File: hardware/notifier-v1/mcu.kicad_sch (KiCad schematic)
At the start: 18 parts, among them SW1 RESET, SW2 BOOT, SW3 BUTTON, U1 ESP32-S3-WROOM-1-N8R2

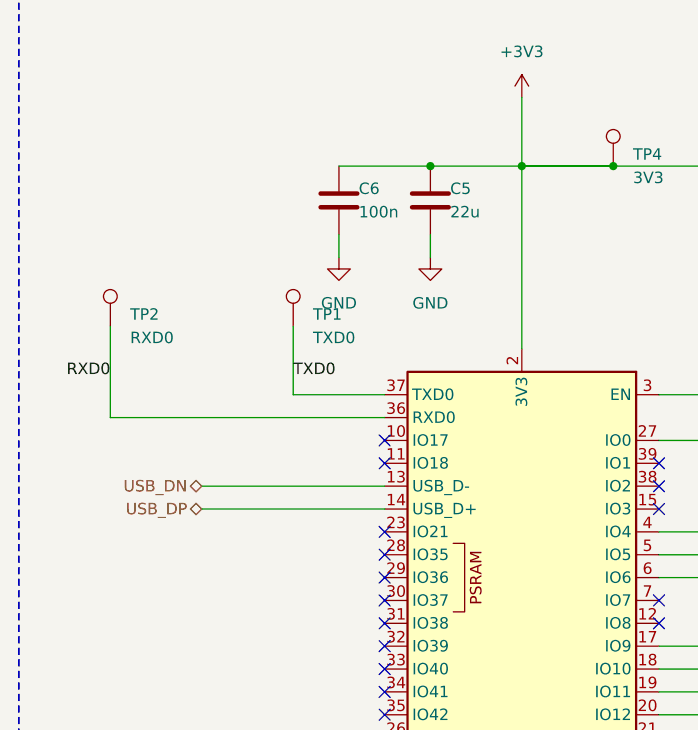
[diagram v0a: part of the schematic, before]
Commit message: notifier-v1: USB 22 ohm series resistors, 1 uF at module 3V3, second buck output cap
Co-Authored-By: Claude Opus 5.5 <noreply@anthropic.com>
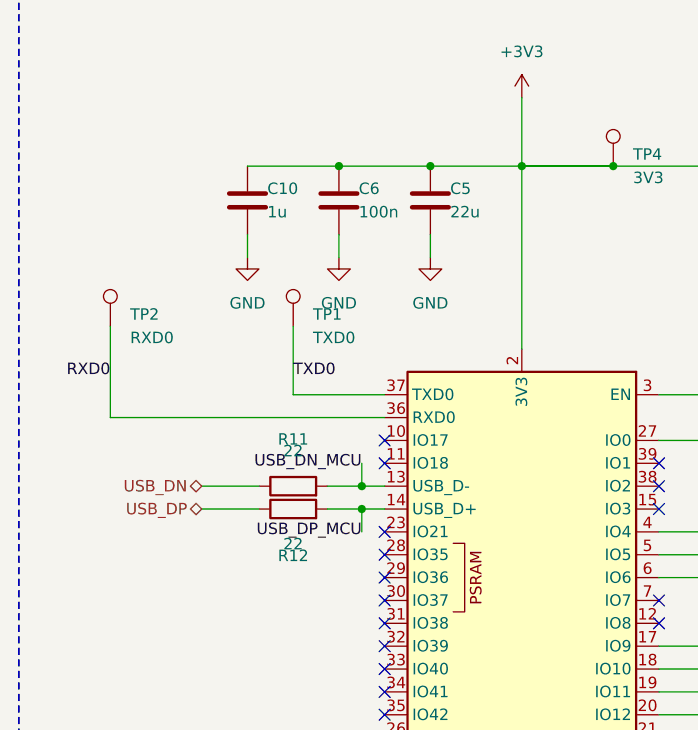
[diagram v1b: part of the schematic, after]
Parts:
- added C10: 1u, Capacitor_SMD:C_0402_1005Metric, symbol Device:C
- added R11, R12: 22, Resistor_SMD:R_0402_1005Metric, symbol Device:R
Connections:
- net +3V3: now also C10.1
- net GND: now also C10.2
- net USB_DN: now also R11.1; no longer U1.13 (USB_D-)
- net USB_DP: now also R12.1; no longer U1.14 (USB_D+)
- new net USB_DN_MCU: R11.2, U1.13 (USB_D-)
- new net USB_DP_MCU: R12.2, U1.14 (USB_D+)
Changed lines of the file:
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@@
+	)
+	(symbol
+		(lib_id "Device:C")
+		(at 172.72 95.25 0)
+		(unit 1)
+		(exclude_from_sim no)
+		(in_bom yes)
+		(on_board yes)
+		(dnp no)
+		(fields_autoplaced no)
+		(property "Reference" "C10"
+			(at 174.92 93.95 0)
+			(effects
+				(font
+					(size 1.27 1.27)
+				) (justify left)
+			)
+		)
+		(property "Value" "1u"
+			(at 174.92 96.55 0)
+			(effects
+				(font
+					(size 1.27 1.27)
+				) (justify left)
+			)
+		)
+		(property "Footprint" "Capacitor_SMD:C_0402_1005Metric"
+			(at 173.6852 91.44 0.0000)
+			(effects
+				(font
+					(size 1.27 1.27)
+				)
+				(hide yes)
+			)
+		)
+		(property "LCSC" "C52923"
+			(at 175.26 100.3299 0)
+			(effects
+				(font
+					(size 1.27 1.27)
+				)
+				(justify left) (hide yes)
+			)
+		)
+		(pin "1"
+		)
+		(pin "2"
+		)
+		(instances
+			(project "notifier-v1"
+				(path "/85cf2753-6181-5f74-b525-c66aecc4c100/8ee93a8b-7827-5c2b-aac9-b7bd720c2d76"
+					(reference "C10")
+					(unit 1)
+				)
+			)
+		)
+	)
+	(symbol
+		(lib_id "power:GND")
+		(at 172.72 101.6 0)
+		(unit 1)
+		(exclude_from_sim no)
+		(in_bom yes)
+		(on_board yes)
+		(dnp no)
+		(fields_autoplaced no)
+		(property "Reference" "#PWR15"
+			(at 172.72 95.25 0.0000)
+			(effects
+				(font
+					(size 1.27 1.27)
+				)
+				(justify left)
+				(hide yes)
+			)
+		)
+		(property "Value" "GND"
+			(at 172.72 106.68 0)
+			(effects
+				(font
+					(size 1.27 1.27)
+				)
+			)
+		)
+		(pin "1"
+		)
+		(instances
+			(project "notifier-v1"
+				(path "/85cf2753-6181-5f74-b525-c66aecc4c100/8ee93a8b-7827-5c2b-aac9-b7bd720c2d76"
+					(reference "#PWR15")
+					(unit 1)
+				)
+			)
+		)
 	)
 	(symbol
@@
 		(dnp no)
 		(fields_autoplaced no)
-		(property "Reference" "#PWR15"
+		(property "Reference" "#PWR16"
 			(at 203.2 171.45 0.0000)
 			(effects
@@
 			(project "notifier-v1"
 				(path "/85cf2753-6181-5f74-b525-c66aecc4c100/8ee93a8b-7827-5c2b-aac9-b7bd720c2d76"
-					(reference "#PWR15")
+					(reference "#PWR16")
 					(unit 1)
 				)
@@
 	)
 	(symbol
+		(lib_id "Device:R")
+		(at 177.8 127 90)
+		(unit 1)
+		(exclude_from_sim no)
+		(in_bom yes)
+		(on_board yes)
+		(dnp no)
+		(fields_autoplaced no)
+		(property "Reference" "R11"
+			(at 177.8 121.8 270)
+			(effects
+				(font
+					(size 1.27 1.27)
+				)
+			)
+		)
+		(property "Value" "22"
+			(at 177.8 123.1 270)
+			(effects
+				(font
+					(size 1.27 1.27)
+				)
+			)
+		)
+		(property "Footprint" "Resistor_SMD:R_0402_1005Metric"
+			(at 176.022 127 90)
+			(effects
+				(font
+					(size 1.27 1.27)
+				)
+				(hide yes)
+			)
+		)
+		(property "LCSC" "C25092"
+			(at 180.34 132.0799 0)
+			(effects
+				(font
+					(size 1.27 1.27)
+				)
+				(justify left) (hide yes)
+			)
+		)
+		(pin "1"
+		)
+		(pin "2"
+		)
+		(instances
+			(project "notifier-v1"
+				(path "/85cf2753-6181-5f74-b525-c66aecc4c100/8ee93a8b-7827-5c2b-aac9-b7bd720c2d76"
+					(reference "R11")
+					(unit 1)
+				)
+			)
+		)
+	)
+	(symbol
+		(lib_id "Device:R")
+		(at 177.8 129.54 90)
+		(unit 1)
+		(exclude_from_sim no)
+		(in_bom yes)
+		(on_board yes)
+		(dnp no)
+		(fields_autoplaced no)
+		(property "Reference" "R12"
+			(at 177.8 134.74 270)
+			(effects
+				(font
+					(size 1.27 1.27)
+				)
+			)
+		)
+		(property "Value" "22"
+			(at 177.8 133.44 270)
+			(effects
+				(font
+					(size 1.27 1.27)
+				)
+			)
+		)
+		(property "Footprint" "Resistor_SMD:R_0402_1005Metric"
+			(at 176.022 129.54 90)
+			(effects
+				(font
+					(size 1.27 1.27)
+				)
+				(hide yes)
+			)
+		)
+		(property "LCSC" "C25092"
+			(at 180.34 134.6199 0)
+			(effects
+				(font
+					(size 1.27 1.27)
+				)
+				(justify left) (hide yes)
+			)
+		)
+		(pin "1"
+		)
+		(pin "2"
+		)
+		(instances
+			(project "notifier-v1"
+				(path "/85cf2753-6181-5f74-b525-c66aecc4c100/8ee93a8b-7827-5c2b-aac9-b7bd720c2d76"
+					(reference "R12")
+					(unit 1)
+				)
+			)
+		)
+	)
+	(symbol
 		(lib_id "Connector:TestPoint")
 		(at 177.8 109.22 0)
@@
 		(dnp no)
 		(fields_autoplaced no)
-		(property "Reference" "#PWR16"
+		(property "Reference" "#PWR17"
 			(at 236.22 107.95 0.0000)
 			(effects
@@
 			(project "notifier-v1"
 				(path "/85cf2753-6181-5f74-b525-c66aecc4c100/8ee93a8b-7827-5c2b-aac9-b7bd720c2d76"
-					(reference "#PWR16")
+					(reference "#PWR17")
 					(unit 1)
 				)
@@
 		(dnp no)
 		(fields_autoplaced no)
-		(property "Reference" "#PWR17"
+		(property "Reference" "#PWR18"
 			(at 246.38 110.49 0.0000)
 			(effects
@@
 			(project "notifier-v1"
 				(path "/85cf2753-6181-5f74-b525-c66aecc4c100/8ee93a8b-7827-5c2b-aac9-b7bd720c2d76"
-					(reference "#PWR17")
+					(reference "#PWR18")
 					(unit 1)
 				)
@@
 		(dnp no)
 		(fields_autoplaced no)
-		(property "Reference" "#PWR18"
+		(property "Reference" "#PWR19"
 			(at 274.32 110.49 0.0000)
 			(effects
@@
 			(project "notifier-v1"
 				(path "/85cf2753-6181-5f74-b525-c66aecc4c100/8ee93a8b-7827-5c2b-aac9-b7bd720c2d76"
-					(reference "#PWR18")
+					(reference "#PWR19")
 					(unit 1)
 				)
@@
 		(dnp no)
 		(fields_autoplaced no)
-		(property "Reference" "#PWR19"
+		(property "Reference" "#PWR20"
 			(at 320.04 110.49 0.0000)
 			(effects
@@
 			(project "notifier-v1"
 				(path "/85cf2753-6181-5f74-b525-c66aecc4c100/8ee93a8b-7827-5c2b-aac9-b7bd720c2d76"
-					(reference "#PWR19")
+					(reference "#PWR20")
 					(unit 1)
 				)
@@
 	(wire (pts (xy 193.04 99.06) (xy 193.04 101.6)) (stroke (width 0) (type default)))
 	(wire (pts (xy 182.88 99.06) (xy 182.88 101.6)) (stroke (width 0) (type default)))
+	(wire (pts (xy 182.88 91.44) (xy 172.72 91.44)) (stroke (width 0) (type default)))
+	(wire (pts (xy 172.72 99.06) (xy 172.72 101.6)) (stroke (width 0) (type default)))
 	(wire (pts (xy 203.2 91.44) (xy 213.36 91.44)) (stroke (width 0) (type default)))
 	(wire (pts (xy 203.2 167.64) (xy 203.2 177.8)) (stroke (width 0) (type default)))
 	(wire (pts (xy 203.2 172.72) (xy 213.36 172.72)) (stroke (width 0) (type default)))
-	(wire (pts (xy 187.96 127.0) (xy 167.64 127.0)) (stroke (width 0) (type default)))
-	(wire (pts (xy 187.96 129.54) (xy 167.64 129.54)) (stroke (width 0) (type default)))
+	(wire (pts (xy 173.99 127.0) (xy 167.64 127.0)) (stroke (width 0) (type default)))
+	(wire (pts (xy 181.61 127.0) (xy 185.42 127.0)) (stroke (width 0) (type default)))
+	(wire (pts (xy 185.42 127.0) (xy 187.96 127.0)) (stroke (width 0) (type default)))
+	(wire (pts (xy 185.42 127.0) (xy 185.42 124.46)) (stroke (width 0) (type default)))
+	(wire (pts (xy 173.99 129.54) (xy 167.64 129.54)) (stroke (width 0) (type default)))
+	(wire (pts (xy 181.61 129.54) (xy 185.42 129.54)) (stroke (width 0) (type default)))
+	(wire (pts (xy 185.42 129.54) (xy 187.96 129.54)) (stroke (width 0) (type default)))
+	(wire (pts (xy 185.42 129.54) (xy 185.42 132.08)) (stroke (width 0) (type default)))
 	(wire (pts (xy 187.96 116.84) (xy 177.8 116.84)) (stroke (width 0) (type default)))
 	(wire (pts (xy 177.8 116.84) (xy 177.8 109.22)) (stroke (width 0) (type default)))
@@
 	(wire (pts (xy 304.8 104.14) (xy 320.04 104.14)) (stroke (width 0) (type default)))
 	(wire (pts (xy 320.04 114.3) (xy 320.04 116.84)) (stroke (width 0) (type default)))
+	(junction (at 182.88 91.44) (diameter 0) (color 0 0 0 0))
+	(junction (at 185.42 127.0) (diameter 0) (color 0 0 0 0))
+	(junction (at 185.42 129.54) (diameter 0) (color 0 0 0 0))
 	(junction (at 193.04 91.44) (diameter 0) (color 0 0 0 0))
 	(junction (at 203.2 91.44) (diameter 0) (color 0 0 0 0))
@@
 	(no_connect (at 218.44 124.46))
 	(hierarchical_label "USB_DN" (shape bidirectional) (at 167.64 127.0 180) (effects (font (size 1.27 1.27)) (justify right)))
+	(label "USB_DN_MCU" (at 185.42 124.46 180) (effects (font (size 1.27 1.27)) (justify right)))
 	(hierarchical_label "USB_DP" (shape bidirectional) (at 167.64 129.54 180) (effects (font (size 1.27 1.27)) (justify right)))
+	(label "USB_DP_MCU" (at 185.42 132.08 180) (effects (font (size 1.27 1.27)) (justify right)))
 	(label "TXD0" (at 177.8 114.3 0) (effects (font (size 1.27 1.27)) (justify left)))
 	(label "RXD0" (at 157.48 114.3 180) (effects (font (size 1.27 1.27)) (justify right)))

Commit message: notifier-v1: 90 ohm USB pair, hand-drawn and locked
USB D+/D- are 0.27 mm with a 0.15 mm gap on F.Cu over the In1 GND plane: 90 ohm
differential on JLC04161H-7628 (prepreg 0.2104 mm, er 4.4, 1 oz, solder mask).
The router left the pair partial (interleaved USB-C pads) and snaked it over
B.Cu with ~8 vias; drawing it in layout_v1.py makes it straight, via-free and
the pipeline passed 4 of 4 runs (was ~1 of 3).

- U2 (USBLC6) rotated 270 for flow-through; VBUS_IN/GND middle pins by via
- module-side nets renamed MCU_USB_DP/MCU_USB_DN (KRT pairs by suffix)
- route_krt.sh: diff stage dropped, --keep-input-copper
- ORDER.md: calculator inputs to verify; hw-layout skill updated

Co-Authored-By: Claude Opus 5.5 <noreply@anthropic.com>
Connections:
- net USB_DN_MCU renamed MCU_USB_DN
- net USB_DP_MCU renamed MCU_USB_DP
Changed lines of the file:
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@@
 	(no_connect (at 218.44 124.46))
 	(hierarchical_label "USB_DN" (shape bidirectional) (at 167.64 127.0 180) (effects (font (size 1.27 1.27)) (justify right)))
-	(label "USB_DN_MCU" (at 185.42 124.46 180) (effects (font (size 1.27 1.27)) (justify right)))
+	(label "MCU_USB_DN" (at 185.42 124.46 180) (effects (font (size 1.27 1.27)) (justify right)))
 	(hierarchical_label "USB_DP" (shape bidirectional) (at 167.64 129.54 180) (effects (font (size 1.27 1.27)) (justify right)))
-	(label "USB_DP_MCU" (at 185.42 132.08 180) (effects (font (size 1.27 1.27)) (justify right)))
+	(label "MCU_USB_DP" (at 185.42 132.08 180) (effects (font (size 1.27 1.27)) (justify right)))
 	(label "TXD0" (at 177.8 114.3 0) (effects (font (size 1.27 1.27)) (justify left)))
 	(label "RXD0" (at 157.48 114.3 180) (effects (font (size 1.27 1.27)) (justify right)))

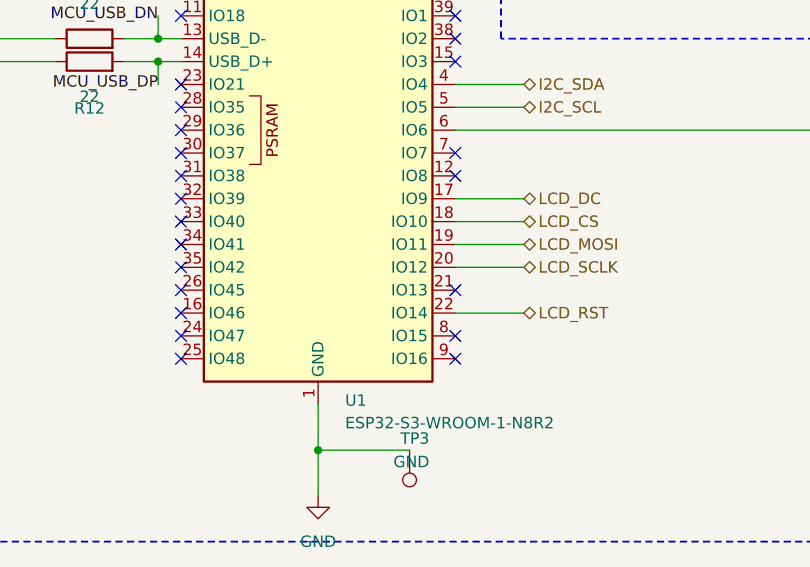
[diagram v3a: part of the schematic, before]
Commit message: Sensor neck: no plane under island/neck, guarded 0.15 mm bus, wider slot
- In1 GND left out under the sensor island and neck; the neck bus is
  3V3 | GND | SDA | SCL | GND at 0.15 mm, guards joined on B.Cu and
  stitched to In1 below the neck
- Module-side slot widened to 1.8 mm (island side stays 1.2 mm)
- Island hand-routed and locked (deterministic, clear of SHT40 keepout)
- C12 4.7u bulk cap where 3V3 enters the island
- R13 33R in series with LCD_SCLK (new net MCU_LCD_SCLK), GND vias
  beside the SPI layer changes where there is room
- In2 island removal drops slivers between the module thermal vias

Co-Authored-By: Claude Opus 5.5 <noreply@anthropic.com>
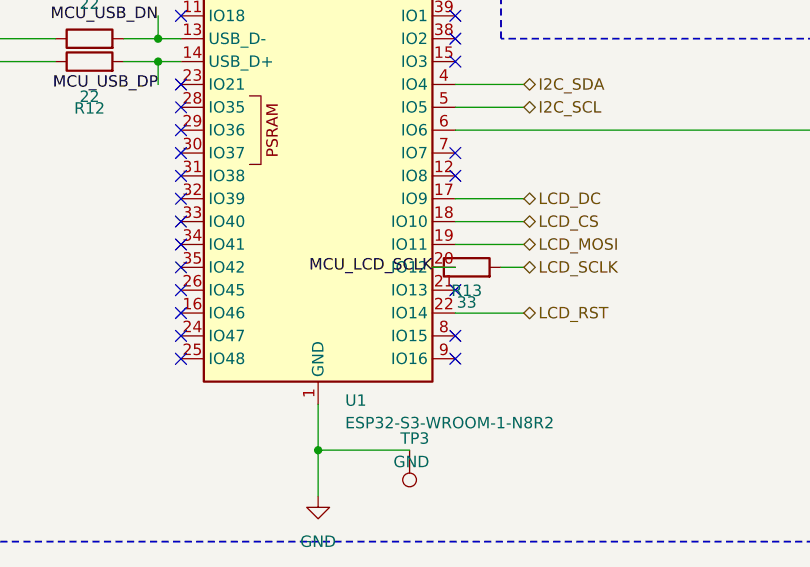
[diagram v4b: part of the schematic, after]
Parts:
- added R13: 33, Resistor_SMD:R_0402_1005Metric, symbol Device:R
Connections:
- net LCD_SCLK: now also R13.2; no longer U1.20 (IO12)
- new net MCU_LCD_SCLK: R13.1, U1.20 (IO12)
